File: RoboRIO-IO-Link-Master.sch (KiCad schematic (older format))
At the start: 43 parts, among them J1 1885650000, J2 XG4H-1031, J3 1885710000, J4 1885710000, J5 1885710000, J6 1885710000, M1 CSD18504Q5A, U1 SI4431BDY-T1-E3, U2 LM3488MMX_NOPB, Y1 ABM3B-14.7456MHZ-10-1-U-T

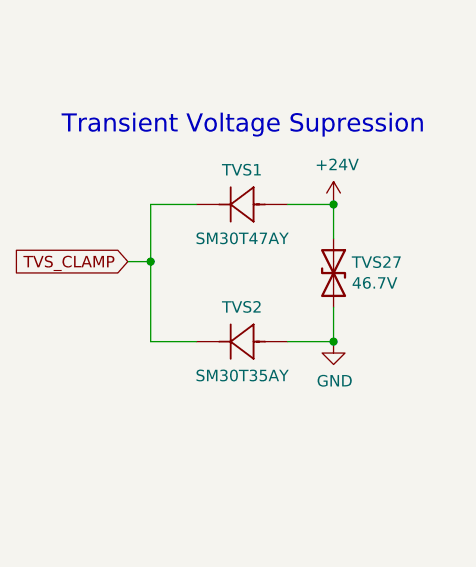
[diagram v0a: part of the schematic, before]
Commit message: Imported and Started Footprint Associations
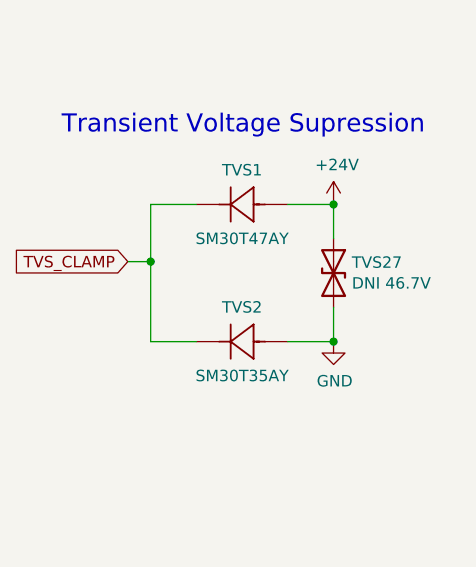
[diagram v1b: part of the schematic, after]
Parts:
- C1: footprint (none) -> UCL1V101MCL6GS:UCL1V101MCL6GS
- C10, C11: footprint (none) -> CL05C050CB5NNNC:CL05C050CB5NNNC
- C2: footprint (none) -> CL10B104KB8NNNC:CL10B104KB8NNNC
- C3, C9: footprint (none) -> CL21B106KOQNNNE:CL21B106KOQNNNE
- C4: footprint (none) -> CL05B102KB5NNNC:CL05B102KB5NNNC
- C5: footprint (none) -> CL03A223KQ3NNNC:CL03A223KQ3NNNC
- C6: footprint (none) -> CL03C100JA3GNNC:CL03C100JA3GNNC
- C7, C8: footprint (none) -> 35SVPF82M:35SVPF82M
- D1: footprint (none) -> FSV10150V:FSV10150V
- D2, D3, D4: footprint (none) -> LTSTC191KRKT:LTSTC191KRKT
- J1: footprint (none) -> 1885650000:1885650000
- J2: footprint (none) -> XG4H1031:XG4H1031
- J3, J4, J5, J6: footprint (none) -> 1885710000:1885710000
- L1: footprint (none) -> 74439346047:74439346047
- TVS27: value 46.7V -> DNI 46.7V
- U1: footprint SOIC-8_SI -> SI4431BDY-T1-E3:SI4431BDY-T1-E3
- U2: footprint MUA08A -> LM3488MMX-NOPB:LM3488MMX-NOPB
- Y1: footprint (none) -> ABM3B14:ABM3B14.7456MHZ101UT
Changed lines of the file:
@@
 F 0 "J2" H 1600 1850 50  0000 C CNN
 F 1 "XG4H-1031" H 1800 1250 50  0000 C CNN
-F 2 "" H 2450 1500 50  0001 C CNN
+F 2 "XG4H1031:XG4H1031" H 2450 1500 50  0001 C CNN
 F 3 "" H 2450 1500 50  0001 C CNN
 	1    1800 1500
@@
 F 0 "J3" H 4250 1050 50  0000 L CNN
 F 1 "1885710000" V 4300 1150 50  0000 L CNN
-F 2 "" H 4250 1450 50  0001 C CNN
+F 2 "1885710000:1885710000" H 4250 1450 50  0001 C CNN
 F 3 "~" H 4250 1450 50  0001 C CNN
 	1    4250 1450
@@
 F 0 "J4" H 4250 2100 50  0000 L CNN
 F 1 "1885710000" V 4300 2200 50  0000 L CNN
-F 2 "" H 4250 2500 50  0001 C CNN
+F 2 "1885710000:1885710000" H 4250 2500 50  0001 C CNN
 F 3 "~" H 4250 2500 50  0001 C CNN
 	1    4250 2500
@@
 F 0 "J5" H 4250 3150 50  0000 L CNN
 F 1 "1885710000" V 4300 3250 50  0000 L CNN
-F 2 "" H 4250 3550 50  0001 C CNN
+F 2 "1885710000:1885710000" H 4250 3550 50  0001 C CNN
 F 3 "~" H 4250 3550 50  0001 C CNN
 	1    4250 3550
@@
 F 0 "J6" H 4250 4200 50  0000 L CNN
 F 1 "1885710000" V 4300 4300 50  0000 L CNN
-F 2 "" H 4250 4600 50  0001 C CNN
+F 2 "1885710000:1885710000" H 4250 4600 50  0001 C CNN
 F 3 "~" H 4250 4600 50  0001 C CNN
 	1    4250 4600
@@
 F 0 "Y1" V 7500 1450 50  0000 L CNN
 F 1 "ABM3B-14.7456MHZ-10-1-U-T" V 7300 1350 32  0000 L CNN
-F 2 "" H 7500 1500 50  0001 C CNN
+F 2 "ABM3B14:ABM3B14.7456MHZ101UT" H 7500 1500 50  0001 C CNN
 F 3 "~" H 7500 1500 50  0001 C CNN
 	1    7500 1500
@@
 F 0 "C1" H 2600 6600 50  0000 L CNN
 F 1 "100uF-160m" V 2550 6150 50  0000 L CNN
-F 2 "" H 2700 6450 50  0001 C CNN
+F 2 "UCL1V101MCL6GS:UCL1V101MCL6GS" H 2700 6450 50  0001 C CNN
 F 3 "~" H 2700 6450 50  0001 C CNN
 	1    2700 6450
@@
 F 0 "C2" H 2900 6550 50  0000 L CNN
 F 1 "100nF-1m" V 2850 6200 50  0000 L CNN
-F 2 "" H 3038 6300 50  0001 C CNN
+F 2 "CL10B104KB8NNNC:CL10B104KB8NNNC" H 3038 6300 50  0001 C CNN
 F 3 "~" H 3000 6450 50  0001 C CNN
 	1    3000 6450
@@
 F 0 "U2" H 4400 6200 60  0000 C CNN
 F 1 "LM3488MMX_NOPB" H 4400 5750 50  0000 C CNN
-F 2 "MUA08A" H 4150 5750 50  0001 C CNN
+F 2 "LM3488MMX-NOPB:LM3488MMX-NOPB" H 4150 5750 50  0001 C CNN
 F 3 "" H 3300 7350 60  0000 C CNN
 	1    3800 6450
@@
 F 0 "C5" H 3915 7046 50  0000 L CNN
 F 1 "22nF" H 3915 6955 50  0000 L CNN
-F 2 "" H 3838 6850 50  0001 C CNN
+F 2 "CL03A223KQ3NNNC:CL03A223KQ3NNNC" H 3838 6850 50  0001 C CNN
 F 3 "~" H 3800 7000 50  0001 C CNN
 	1    3800 7000
@@
 F 0 "L1" H 5000 6200 50  0000 C CNN
 F 1 "4.7uH-13m" H 5000 6050 50  0000 C CNN
-F 2 "" H 5000 6100 50  0001 C CNN
+F 2 "74439346047:74439346047" H 5000 6100 50  0001 C CNN
 F 3 "~" H 5000 6100 50  0001 C CNN
 	1    5000 6100
@@
 F 0 "C6" H 5165 7446 50  0000 L CNN
 F 1 "10pF" H 5165 7355 50  0000 L CNN
-F 2 "" H 5088 7250 50  0001 C CNN
+F 2 "CL03C100JA3GNNC:CL03C100JA3GNNC" H 5088 7250 50  0001 C CNN
 F 3 "~" H 5050 7400 50  0001 C CNN
 	1    5050 7400
@@
 F 0 "D1" H 6000 6000 50  0000 C CNN
 F 1 "950mV-10A" H 6000 6200 50  0000 C CNN
-F 2 "" H 6000 6100 50  0001 C CNN
+F 2 "FSV10150V:FSV10150V" H 6000 6100 50  0001 C CNN
 F 3 "~" H 6000 6100 50  0001 C CNN
 	1    6000 6100
@@
 F 0 "C7" H 6250 6500 50  0000 L CNN
 F 1 "82uF-20m" V 6100 6100 50  0000 L CNN
-F 2 "" H 6250 6400 50  0001 C CNN
+F 2 "35SVPF82M:35SVPF82M" H 6250 6400 50  0001 C CNN
 F 3 "~" H 6250 6400 50  0001 C CNN
 	1    6250 6400
@@
 F 0 "C8" H 6550 6500 50  0000 L CNN
 F 1 "82uF-20m" V 6400 6100 50  0000 L CNN
-F 2 "" H 6550 6400 50  0001 C CNN
+F 2 "35SVPF82M:35SVPF82M" H 6550 6400 50  0001 C CNN
 F 3 "~" H 6550 6400 50  0001 C CNN
 	1    6550 6400
@@
 	1    0    0    -1
 $EndComp
-$Comp
-L Device:R_US R9
-U 1 1 60900292
-P 9400 3800
-F 0 "R9" V 9350 3650 50  0000 C CNN
-F 1 "1.5k" V 9500 3800 50  0000 C CNN
-F 2 "" V 9440 3790 50  0001 C CNN
-F 3 "~" H 9400 3800 50  0001 C CNN
-	1    9400 3800
-	0    1    1    0
-$EndComp
 Wire Wire Line
 	8600 3800 8750 3800
@@
 Wire Wire Line
 	8600 4300 8750 4300
-$Comp
-L Device:R_US R10
-U 1 1 6091E19D
-P 9400 4050
-F 0 "R10" V 9350 3900 50  0000 C CNN
-F 1 "10k" V 9500 4050 50  0000 C CNN
-F 2 "" V 9440 4040 50  0001 C CNN
-F 3 "~" H 9400 4050 50  0001 C CNN
-	1    9400 4050
-	0    1    1    0
-$EndComp
-$Comp
-L Device:R_US R11
-U 1 1 6091E71B
-P 9400 4300
-F 0 "R11" V 9350 4150 50  0000 C CNN
-F 1 "22k" V 9500 4300 50  0000 C CNN
-F 2 "" V 9440 4290 50  0001 C CNN
-F 3 "~" H 9400 4300 50  0001 C CNN
-	1    9400 4300
-	0    1    1    0
-$EndComp
 Wire Wire Line
 	9050 3800 9250 3800
@@
 	1    0    0    -1
 $EndComp
-$Comp
-L Device:D_TVS TVS27
-U 1 1 607A8AAC
-P 10050 1850
-F 0 "TVS27" V 10004 1930 50  0000 L CNN
-F 1 "46.7V" V 10095 1930 50  0000 L CNN
-F 2 "" H 10050 1850 50  0001 C CNN
-F 3 "~" H 10050 1850 50  0001 C CNN
-	1    10050 1850
-	0    1    1    0
-$EndComp
-Wire Wire Line
-	10050 2000 10050 2150
 Connection ~ 10050 2150
 Connection ~ 10050 1550
@@
 Wire Wire Line
 	9250 1800 9250 2150
-Wire Wire Line
-	10050 1550 10050 1700
 Wire Wire Line
 	9250 1550 9250 1800
@@
 F 0 "C10" H 6850 1200 50  0000 C CNN
 F 1 "5pF" H 6850 1400 50  0000 C CNN
-F 2 "" H 6988 1150 50  0001 C CNN
+F 2 "CL05C050CB5NNNC:CL05C050CB5NNNC" H 6988 1150 50  0001 C CNN
 F 3 "~" H 6950 1300 50  0001 C CNN
 	1    6950 1300
@@
 F 0 "C11" H 7050 1600 50  0000 C CNN
 F 1 "5pF" H 6850 1800 50  0000 C CNN
-F 2 "" H 6988 1550 50  0001 C CNN
+F 2 "CL05C050CB5NNNC:CL05C050CB5NNNC" H 6988 1550 50  0001 C CNN
 F 3 "~" H 6950 1700 50  0001 C CNN
 	1    6950 1700
@@
 F 0 "C3" H 3200 6550 50  0000 L CNN
 F 1 "10uF" V 3150 6350 50  0000 L CNN
-F 2 "" H 3338 6300 50  0001 C CNN
+F 2 "CL21B106KOQNNNE:CL21B106KOQNNNE" H 3338 6300 50  0001 C CNN
 F 3 "~" H 3300 6450 50  0001 C CNN
 	1    3300 6450
@@
 F 0 "C4" V 3600 6700 50  0000 L CNN
 F 1 "1nF" V 3700 6650 50  0000 L CNN
-F 2 "" H 3688 6700 50  0001 C CNN
+F 2 "CL05B102KB5NNNC:CL05B102KB5NNNC" H 3688 6700 50  0001 C CNN
 F 3 "~" H 3650 6850 50  0001 C CNN
 	1    3650 6850
@@
 F 0 "U1" H 2600 6100 50  0000 C CNN
 F 1 "SI4431BDY-T1-E3" H 2550 6600 47  0000 C CNN
-F 2 "SOIC-8_SI" H 3050 6740 60  0001 C CNN
+F 2 "SI4431BDY-T1-E3:SI4431BDY-T1-E3" H 3050 6740 60  0001 C CNN
 F 3 "" H 2150 6500 60  0000 C CNN
 	1    2150 6500
@@
 F 0 "C9" H 6965 6446 50  0000 L CNN
 F 1 "10uF" H 6965 6355 50  0000 L CNN
-F 2 "" H 6888 6250 50  0001 C CNN
+F 2 "CL21B106KOQNNNE:CL21B106KOQNNNE" H 6888 6250 50  0001 C CNN
 F 3 "~" H 6850 6400 50  0001 C CNN
 	1    6850 6400
@@
 F 0 "J1" H 850 6550 50  0000 L CNN
 F 1 "1885650000" H 500 6350 50  0000 L CNN
-F 2 "" H 800 6600 50  0001 C CNN
+F 2 "1885650000:1885650000" H 800 6600 50  0001 C CNN
 F 3 "~" H 800 6600 50  0001 C CNN
 	1    800  6600
@@
 F 0 "D2" H 9050 3750 50  0000 C CNN
 F 1 "RED" H 8750 3850 50  0000 C CNN
-F 2 "" H 8900 3800 50  0001 C CNN
+F 2 "LTSTC191KRKT:LTSTC191KRKT" H 8900 3800 50  0001 C CNN
 F 3 "~" H 8900 3800 50  0001 C CNN
 	1    8900 3800
@@
 F 0 "D3" H 9050 4000 50  0000 C CNN
 F 1 "RED" H 8750 4100 50  0000 C CNN
-F 2 "" H 8900 4050 50  0001 C CNN
+F 2 "LTSTC191KRKT:LTSTC191KRKT" H 8900 4050 50  0001 C CNN
 F 3 "~" H 8900 4050 50  0001 C CNN
 	1    8900 4050
@@
 F 0 "D4" H 9050 4250 50  0000 C CNN
 F 1 "RED" H 8750 4350 50  0000 C CNN
-F 2 "" H 8900 4300 50  0001 C CNN
+F 2 "LTSTC191KRKT:LTSTC191KRKT" H 8900 4300 50  0001 C CNN
 F 3 "~" H 8900 4300 50  0001 C CNN
 	1    8900 4300
 	-1   0    0    1
 $EndComp
+Wire Wire Line
+	10050 1550 10050 1700
+Wire Wire Line
+	10050 2000 10050 2150
+$Comp
+L Device:D_TVS TVS27
+U 1 1 607A8AAC
+P 10050 1850
+F 0 "TVS27" V 10004 1930 50  0000 L CNN
+F 1 "DNI 46.7V" V 10095 1930 50  0000 L CNN
+F 2 "" H 10050 1850 50  0001 C CNN
+F 3 "~" H 10050 1850 50  0001 C CNN
+	1    10050 1850
+	0    1    1    0
+$EndComp
+$Comp
+L Device:R_US R9
+U 1 1 60900292
+P 9400 3800
+F 0 "R9" V 9350 3650 50  0000 C CNN
+F 1 "1.5k" V 9500 3800 50  0000 C CNN
+F 2 "" V 9440 3790 50  0001 C CNN
+F 3 "~" H 9400 3800 50  0001 C CNN
+	1    9400 3800
+	0    1    1    0
+$EndComp
+$Comp
+L Device:R_US R10
+U 1 1 6091E19D
+P 9400 4050
+F 0 "R10" V 9350 3900 50  0000 C CNN
+F 1 "10k" V 9500 4050 50  0000 C CNN
+F 2 "" V 9440 4040 50  0001 C CNN
+F 3 "~" H 9400 4050 50  0001 C CNN
+	1    9400 4050
+	0    1    1    0
+$EndComp
+$Comp
+L Device:R_US R11
+U 1 1 6091E71B
+P 9400 4300
+F 0 "R11" V 9350 4150 50  0000 C CNN
+F 1 "22k" V 9500 4300 50  0000 C CNN
+F 2 "" V 9440 4290 50  0001 C CNN
+F 3 "~" H 9400 4300 50  0001 C CNN
+	1    9400 4300
+	0    1    1    0
+$EndComp
 $EndSCHEMATC

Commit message: PCB/Footprint Work
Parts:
- removed J2: XG4H-1031, XG4H1031:XG4H1031, symbol CustomSymbols:RoboRIO-SPI
- removed J3, J4, J5, J6: 1885710000, 1885710000:1885710000, symbol Connector:Conn_01x08_Female
- added J2: SFH11-PBPC-D17-ST-BK, SFH11-PBPC-D17-ST-BK:SFH11-PBPC-D17-ST-BK, symbol Connector_Generic:Conn_02x17_Odd_Even
- added J3, J4: 1885790000, 1885790000:1885790000, symbol Connector:Conn_01x16_Female
- D2: value RED -> 3.3V
- D3: value RED -> 12V
- D4: value RED -> 24V
- M1: footprint TRANS_NexFET_Q5A -> CSD18504Q5A:CSD18504Q5A
- R1: footprint (none) -> RC0603FR074K42L:RC0603FR074K42L
- R10, R8: footprint (none) -> RC0603FR0710KL:RC0603FR0710KL
- R11: footprint (none) -> RC0603JR0722KL:RC0603JR0722KL
- R2: footprint (none) -> RC0603FR071KL:RC0603FR071KL
- R3: footprint (none) -> RC0603FR0718K2L:RC0603FR0718K2L
- R4: footprint (none) -> RC0603FR0726K1L:RC0603FR0726K1L
- R5: footprint (none) -> RC0603JR07100RL:RC0603JR07100RL
- R6: footprint (none) -> CRCW06030000Z0EBC:CRCW06030000Z0EBC
- R7: footprint (none) -> PMR10EZPFU6L00:PMR10EZPFU6L00
- R9: footprint (none) -> RC0603JR071K5L:RC0603JR071K5L
- TP1: footprint (none) -> RoboRIO-IO-Link-Master:TestPointFootprint
- TP2: value +12V -> 12V; footprint (none) -> RoboRIO-IO-Link-Master:TestPointFootprint
- TP3: value +24V -> 24V; footprint (none) -> RoboRIO-IO-Link-Master:TestPointFootprint
- TVS1: footprint CR_T12AY_STM -> SM30T47AY:SM30T47AY
- TVS2: footprint CR_T12AY_STM -> SM30T35AY:SM30T35AY
- TVS27: footprint (none) -> SMCJ40A-TR:SMCJ40A-TR
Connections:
- net +3V3: now also J2.33 (Pin_33)
- net +5V: now also J2.1 (Pin_1)
- net DCQ0: now also J3.14 (Pin_14)
- net DCQ1: now also J3.10 (Pin_10)
- net DCQ2: now also J3.6 (Pin_6)
- net DCQ3: now also J3.2 (Pin_2)
- net DCQ4: now also J4.14 (Pin_14)
- net DCQ5: now also J4.10 (Pin_10)
- net DCQ6: now also J4.6 (Pin_6)
- net DCQ7: now also J4.2 (Pin_2)
- net DDI0: now also J3.13 (Pin_13)
- net DDI1: now also J3.9 (Pin_9)
- net DDI2: now also J3.5 (Pin_5)
- net DDI3: now also J3.1 (Pin_1)
- net DDI4: now also J4.13 (Pin_13)
- net DDI5: now also J4.9 (Pin_9)
- net DDI6: now also J4.5 (Pin_5)
- net DDI7: now also J4.1 (Pin_1)
- net DL+0: now also J3.15 (Pin_15)
- net DL+1: now also J3.11 (Pin_11)
- net DL+2: now also J3.7 (Pin_7)
- net DL+3: now also J3.3 (Pin_3)
- net DL+4: now also J4.15 (Pin_15)
- net DL+5: now also J4.11 (Pin_11)
- net DL+6: now also J4.7 (Pin_7)
- net DL+7: now also J4.3 (Pin_3)
- net GND: now also J2.12 (Pin_12), J2.16 (Pin_16), J2.20 (Pin_20), J2.24 (Pin_24), J2.28 (Pin_28), J2.30 (Pin_30), J2.6 (Pin_6), J2.8 (Pin_8), J3.12 (Pin_12), J3.16 (Pin_16), J3.4 (Pin_4), J3.8 (Pin_8), J4.12 (Pin_12), J4.16 (Pin_16), J4.4 (Pin_4), J4.8 (Pin_8)
- new net MXP-CS: J2.19 (Pin_19)
- new net MXP-DIO0: J2.11 (Pin_11)
- new net MXP-MISO: J2.23 (Pin_23)
- new net MXP-MOSI: J2.25 (Pin_25)
- new net MXP-SCLK: J2.21 (Pin_21)
- no-connect marks 7 -> 26
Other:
- note added: "RoboRIO MXP Jack\n"
- note removed: "RoboRIO SPI Jack\n"
- moved on the sheet: C10, C11, D2, D3, D4, R10, R11, R8, R9, TVS1, TVS2, TVS27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

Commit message: More PCB Layout
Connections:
- net Dual IO-Link Master1/CLKI: no longer R8.2
- net Dual IO-Link Master1/XI: no longer C11.2, Y1.3
- net Dual IO-Link Master1/XO: no longer C10.1, Y1.1
- net Dual IO-Link Master4/XI: now also C11.2, Y1.3
- net Dual IO-Link Master4/XO: now also C10.1, Y1.1
- net MXP-DIO0: no longer names the net of J2.11 (Pin_11)
- new net Dual IO-Link Master4/CLKI: R8.2
- no-connect marks 26 -> 27

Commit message: Wrapping up first prototype
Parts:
- added R80, R81, R82: 1k, RC0603FR071KL:RC0603FR071KL, symbol Device:R_US
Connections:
- net Dual IO-Link Master1/CLKI: now also R82.2
- net Dual IO-Link Master2/CLKI: now also R80.2
- net Dual IO-Link Master2/CLKO: now also R81.1
- new net Dual IO-Link Master3/CLKI: R81.2
- new net Dual IO-Link Master3/CLKO: R82.1
- new net Dual IO-Link Master4/CLKO: R80.1
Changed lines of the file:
@@
 	6250 3900 6500 3900
 Wire Wire Line
-	6500 3900 6500 4850
+	6500 3900 6500 4500
 Wire Wire Line
 	6500 4850 6250 4850
@@
 	6250 3800 6500 3800
 Wire Wire Line
-	6500 3800 6500 2850
+	6500 3800 6500 3750
 Wire Wire Line
 	6500 2850 6250 2850
@@
 	6250 2750 6500 2750
 Wire Wire Line
-	6500 2750 6500 1800
+	6500 2750 6500 2700
 Wire Wire Line
 	6500 1800 6250 1800
@@
 P 6650 3350
 F 0 "#PWR055" H 6650 3100 50  0001 C CNN
-F 1 "GND" H 6655 3177 50  0000 C CNN
+F 1 "GND" H 6650 3200 50  0000 C CNN
 F 2 "" H 6650 3350 50  0001 C CNN
 F 3 "" H 6650 3350 50  0001 C CNN
@@
 $EndComp
 NoConn ~ 2550 2150
+$Comp
+L Device:R_US R82
+U 1 1 608915DE
+P 6500 4650
+F 0 "R82" H 6568 4696 50  0000 L CNN
+F 1 "1k" H 6568 4605 50  0000 L CNN
+F 2 "RC0603FR071KL:RC0603FR071KL" V 6540 4640 50  0001 C CNN
+F 3 "~" H 6500 4650 50  0001 C CNN
+	1    6500 4650
+	1    0    0    -1
+$EndComp
+Wire Wire Line
+	6500 4800 6500 4850
+$Comp
+L Device:R_US R81
+U 1 1 60893D27
+P 6500 3600
+F 0 "R81" H 6300 3650 50  0000 L CNN
+F 1 "1k" H 6350 3550 50  0000 L CNN
+F 2 "RC0603FR071KL:RC0603FR071KL" V 6540 3590 50  0001 C CNN
+F 3 "~" H 6500 3600 50  0001 C CNN
+	1    6500 3600
+	1    0    0    -1
+$EndComp
+Wire Wire Line
+	6500 3450 6500 2850
+$Comp
+L Device:R_US R80
+U 1 1 60896555
+P 6500 2550
+F 0 "R80" H 6568 2596 50  0000 L CNN
+F 1 "1k" H 6568 2505 50  0000 L CNN
+F 2 "RC0603FR071KL:RC0603FR071KL" V 6540 2540 50  0001 C CNN
+F 3 "~" H 6500 2550 50  0001 C CNN
+	1    6500 2550
+	1    0    0    -1
+$EndComp
+Wire Wire Line
+	6500 2400 6500 1800
 $EndSCHEMATC
